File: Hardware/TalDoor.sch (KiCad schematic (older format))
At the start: 57 parts, among them J1 SI-52003-F_RJ45, J2 Screw_Terminal_01x02, J3 Conn_01x06_Male, J4 Conn_01x06_Male, P1 PocketBeagle, Q1 RK7002BM, Q2 BSS223PWH6327XTSA1, U1 DRV8837, U2 ENC28J60-I/SO, U3 PN532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

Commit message: Added 5v motor control. Updated schematic, images, BOM, PCB layout
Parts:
- added C17, C18, C19: 1uF, Capacitors_SMD:C_0603, symbol C
- added U5: CAT3200-5, TO_SOT_Packages_SMD:SOT-23-6, symbol CAT3200-5
- J2: footprint Pin_Headers:Pin_Header_Angled_1x02_Pitch2.54mm -> Pin_Headers:Pin_Header_Straight_1x02_Pitch2.54mm
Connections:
- wire segments 222 -> 237
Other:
- note added: "Motor 5v"
- note removed: "May need \nto be 5v"
- moved on the sheet: C1, C8, U1

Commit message: Started changed base on Hardware 1 build
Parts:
- removed C18, C19: 1uF, Capacitors_SMD:C_0603, symbol C
- removed J2: Screw_Terminal_01x02, Pin_Headers:Pin_Header_Straight_1x02_Pitch2.54mm, symbol Screw_Terminal_01x02
- removed U5: CAT3200-5, TO_SOT_Packages_SMD:SOT-23-6, symbol CAT3200-5
- added J2: Conn_01x02, Pin_Headers:Pin_Header_Straight_1x02_Pitch2.54mm, symbol Conn_01x02
- added U5: NCP1117-3.3_SOT223, TO_SOT_Packages_SMD:SOT-223-3_TabPin2, symbol NCP1117-3.3_SOT223
- C17: value 1uF -> 10uF; footprint Capacitors_SMD:C_0603 -> Capacitors_SMD:C_0805
- U1: footprint Housings_SON:WSON-8_1EP_2x2mm_Pitch0.5mm_ThermalVias -> TalDoor_Footprints:WSON-8_1EP_2x2mm_Pitch0.5mm_ThermalVias
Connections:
- net labels added: +5V
- wire segments 237 -> 220
- no-connect marks 12 -> 17
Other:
- note added: "3.3v Supply"
- note added: "Each VDD pin gets \n0.1uF cap to GND\n"
- note added: "MOSI/MISO may need to be changed\nper PB Testing"
- note added: "Place close \nto C12&13"
- note removed: "Each VDD pin gets 0.1uF cap to GND\n"
- note removed: "For Net conn"
- note removed: "Motor 5v"
- note removed: "VBat+"
- note removed: "Vref+"
- moved on the sheet: BZ1, C1, C10, C11, C14, C16, C2, C3, C4, C5, C6, C7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

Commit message: Updating PCB layout, unfinished
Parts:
- C15: value 1000uF -> 470uF
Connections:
- no-connect marks 17 -> 11
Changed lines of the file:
@@
 P 5900 1750
 F 0 "C15" H 5925 1850 50  0000 L CNN
-F 1 "1000uF" H 5925 1650 50  0000 L CNN
+F 1 "470uF" H 5925 1650 50  0000 L CNN
 F 2 "Capacitors_THT:CP_Radial_D10.0mm_P5.00mm" H 5900 1750 50  0001 C CNN
 F 3 "" H 5900 1750 50  0001 C CNN
@@
 	1    0    0    -1
 $EndComp
-NoConn ~ 9950 1800
-NoConn ~ 9350 1900
-NoConn ~ 9350 2200
 $Comp
 L PocketBeagle P1
@@
 	1    0    0    -1
 $EndComp
-NoConn ~ 8500 1900
-NoConn ~ 8500 2000
-NoConn ~ 8500 2200
 $Comp
 L +5V #PWR014

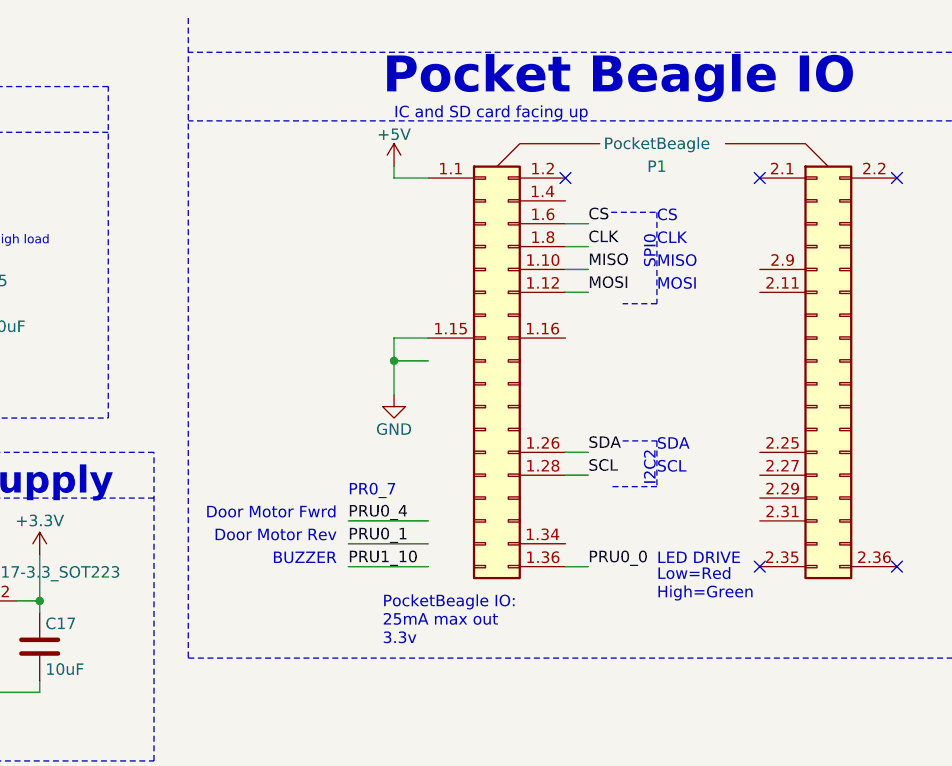
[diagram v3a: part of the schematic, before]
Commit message: Updated PCB layout for fixes from v1
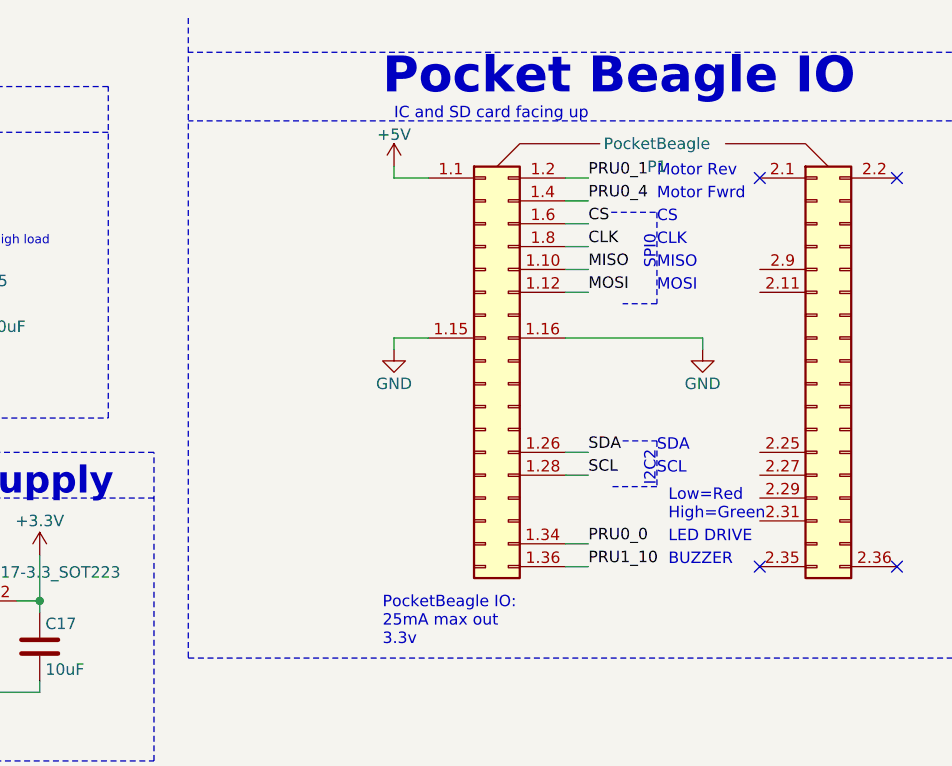
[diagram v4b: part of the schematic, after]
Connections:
- net GND: now also P1.1.16 (PIN_16)
- net PRU0_0: now also P1.1.34 (Pin_34); no longer P1.1.36 (Pin_36)
- net PRU0_1: now also P1.1.2 (Pin_2)
- net PRU0_4: now also P1.1.4 (Pin_4)
- net PRU1_10: now also P1.1.36 (Pin_36)
- no-connect marks 11 -> 10
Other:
- note added: "Motor Fwrd"
- note added: "Motor Rev"
- note removed: "Door Motor Rev"
- note removed: "PR0_7"
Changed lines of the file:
@@
 L GND #PWR06
 U 1 1 5A47602A
-P 7750 2150
-F 0 "#PWR06" H 7750 1900 50  0001 C CNN
-F 1 "GND" H 7750 2000 50  0000 C CNN
-F 2 "" H 7750 2150 50  0001 C CNN
-F 3 "" H 7750 2150 50  0001 C CNN
-	1    7750 2150
-	1    0    0    -1
-$EndComp
-Text Label 7550 2900 0    50   ~ 0
+P 7750 1950
+F 0 "#PWR06" H 7750 1700 50  0001 C CNN
+F 1 "GND" H 7750 1800 50  0000 C CNN
+F 2 "" H 7750 1950 50  0001 C CNN
+F 3 "" H 7750 1950 50  0001 C CNN
+	1    7750 1950
+	1    0    0    -1
+$EndComp
+Text Label 8600 2900 0    50   ~ 0
 PRU1_10
-Text Label 7550 2800 0    50   ~ 0
+Text Label 8600 1200 0    50   ~ 0
 PRU0_1
-Text Label 7550 2700 0    50   ~ 0
+Text Label 8600 1300 0    50   ~ 0
 PRU0_4
 Text Notes 7700 3250 0    50   ~ 0
 PocketBeagle IO:\n25mA max out\n3.3v
-Text Notes 7500 2900 2    50   ~ 0
+Text Notes 8950 2900 0    50   ~ 0
 BUZZER
-Text Notes 7500 2700 2    50   ~ 0
-Door Motor Fwrd
-Text Notes 7500 2800 2    50   ~ 0
-Door Motor Rev
+Text Notes 8900 1300 0    50   ~ 0
+Motor Fwrd
+Text Notes 8900 1200 0    50   ~ 0
+Motor Rev
 $Comp
 L LED D2
@@
 	1    0    0    1
 $EndComp
-Text Notes 8900 2900 0    50   ~ 0
+Text Notes 8950 2800 0    50   ~ 0
 LED DRIVE
-Text Label 8600 2900 0    50   ~ 0
+Text Label 8600 2800 0    50   ~ 0
 PRU0_0
 Text Label 2500 7100 0    50   ~ 0
 PRU0_4
-Text Notes 8900 3050 0    50   ~ 0
+Text Notes 8950 2700 0    50   ~ 0
 Low=Red\nHigh=Green
 $Comp
@@
 Text Label 6400 4600 1    50   ~ 0
 PRU1_10
-Text Notes 7550 2600 0    50   ~ 0
-PR0_7
 $Comp
 L LED D4
@@
 NoConn ~ 9350 1200
 NoConn ~ 9950 1200
-NoConn ~ 8500 1200
 $Bitmap
 Pos 10200 7050
@@
 Wire Wire Line
 	1350 6900 1400 6900
-Connection ~ 7750 2000
-Wire Wire Line
-	7900 2000 7750 2000
-Wire Wire Line
-	7750 1900 7750 2150
 Wire Wire Line
 	7750 1200 7750 1150
@@
 	9400 5850 9300 5850
 Wire Wire Line
-	7900 2700 7550 2700
-Wire Wire Line
-	7900 2800 7550 2800
-Wire Wire Line
-	7900 2900 7550 2900
-Wire Wire Line
 	7900 1900 7750 1900
 Wire Wire Line
@@
 Wire Wire Line
 	2400 3550 2250 3550
-Wire Wire Line
-	8500 1700 8600 1700
 Wire Wire Line
 	8500 1600 8600 1600
@@
 Text Notes 5250 3200 0    39   ~ 0
 Place close \nto C12&13
+Wire Wire Line
+	8500 2800 8600 2800
+Wire Wire Line
+	8500 1200 8600 1200
+Wire Wire Line
+	8500 1300 8600 1300
+Wire Wire Line
+	7750 1900 7750 1950
+$Comp
+L GND #PWR019
+U 1 1 5A8162E6
+P 9100 1950
+F 0 "#PWR019" H 9100 1700 50  0001 C CNN
+F 1 "GND" H 9100 1800 50  0000 C CNN
+F 2 "" H 9100 1950 50  0001 C CNN
+F 3 "" H 9100 1950 50  0001 C CNN
+	1    9100 1950
+	1    0    0    -1
+$EndComp
+Wire Wire Line
+	9100 1900 9100 1950
+Wire Wire Line
+	8500 1900 9100 1900
+Wire Wire Line
+	8500 1700 8600 1700
 $EndSCHEMATC

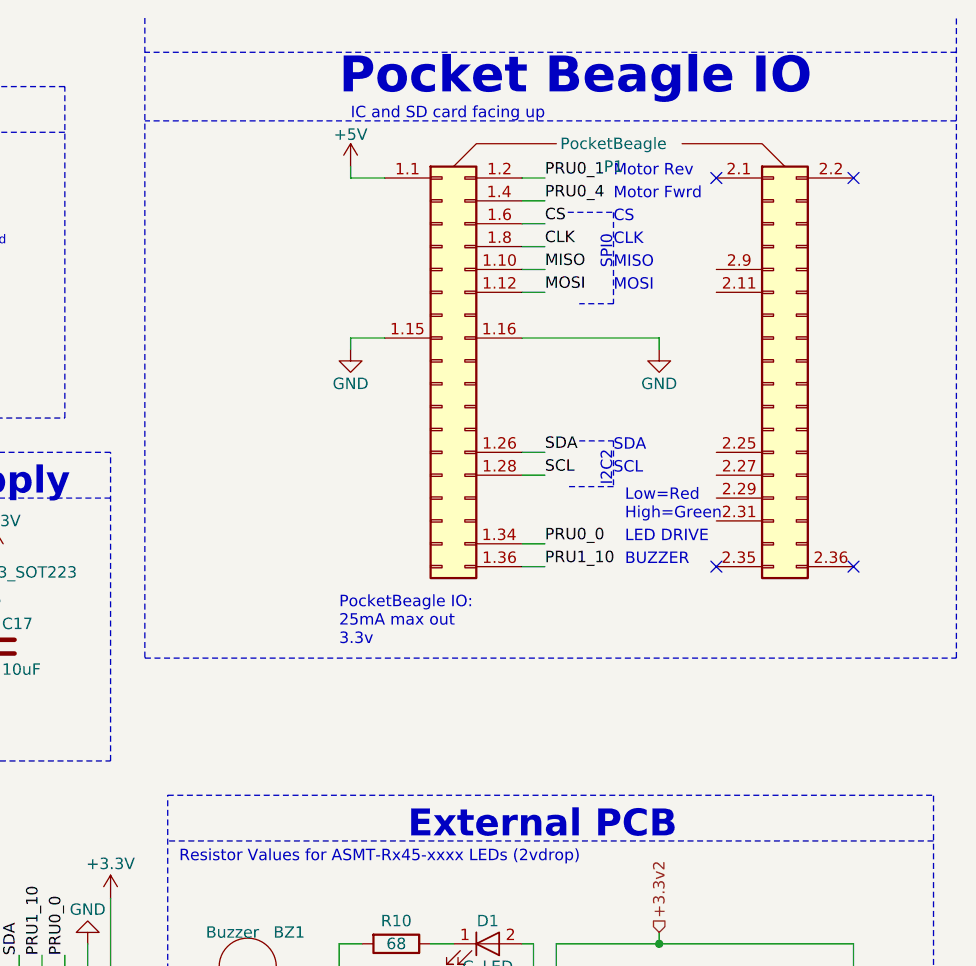
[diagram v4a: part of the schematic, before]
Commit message: Updated PCB with solder jumpers for easier developing
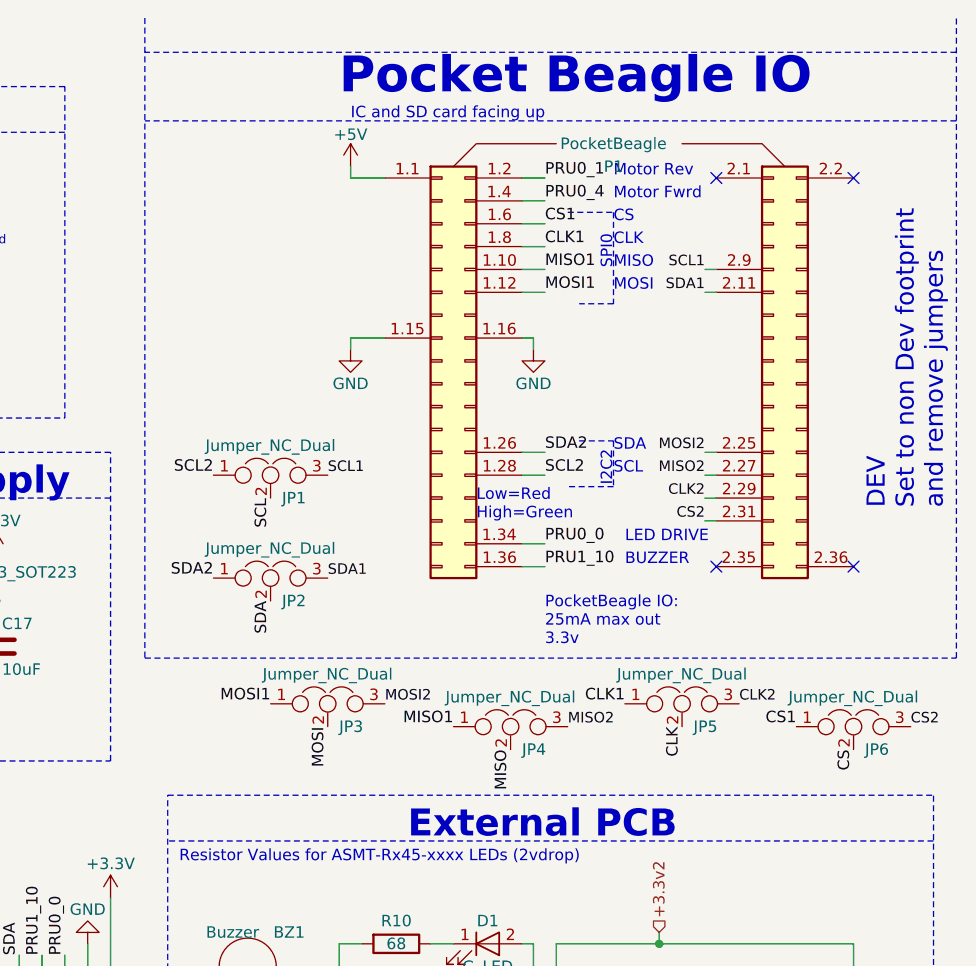
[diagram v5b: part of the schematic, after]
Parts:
- added JP1, JP2, JP3, JP4, JP5, JP6: Jumper_NC_Dual, Connectors:GS3, symbol Jumper_NC_Dual
- P1: footprint TalDoor_Footprints:PocketBeagle_TalDoor -> TalDoor_Footprints:PocketBeagle_DEV_TalDoor
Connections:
- net CLK: now also JP5.2; no longer P1.1.8 (Pin_8)
- net CS: now also JP6.2; no longer P1.1.6 (Pin_6)
- net MISO: now also JP4.2; no longer P1.1.10 (Pin_10)
- net MOSI: now also JP3.2; no longer P1.1.12 (Pin_12)
- net SCL: now also JP1.2; no longer P1.1.28 (Pin_28)
- net SDA: now also JP2.2; no longer P1.1.26 (Pin_26)
- net SDA1: now reaches P1.2.11 (Pin_11)
- net SDA1: now also JP2.3
- net MOSI2: now reaches P1.2.25 (Pin_25)
- net MOSI2: now also JP3.3
- net MISO2: now reaches P1.2.27 (Pin_27)
- net MISO2: now also JP4.3
- net CLK2: now reaches P1.2.29 (Pin_29)
- net CLK2: now also JP5.3
- net CS2: now reaches P1.2.31 (Pin_31)
- net CS2: now also JP6.3
- net SCL1: now reaches P1.2.9 (Pin_9)
- net SCL1: now also JP1.3
- new net CLK1: JP5.1, P1.1.8 (Pin_8)
- new net CS1: JP6.1, P1.1.6 (Pin_6)
- new net MISO1: JP4.1, P1.1.10 (Pin_10)
- new net MOSI1: JP3.1, P1.1.12 (Pin_12)
- new net SCL2: JP1.1, P1.1.28 (Pin_28)
- new net SDA2: JP2.1, P1.1.26 (Pin_26)
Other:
- note added: "DEV\nSet to non Dev footprint\nand remove jumpers\n"
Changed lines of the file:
@@
 CLK
 Text Label 8600 1500 0    50   ~ 0
-CLK
+CLK1
 Text Label 8600 1400 0    50   ~ 0
-CS
+CS1
 Text Label 8600 1600 0    50   ~ 0
-MISO
+MISO1
 Text Label 8600 1700 0    50   ~ 0
-MOSI
+MOSI1
 Text Notes 8900 1600 0    50   ~ 0
 MISO
@@
 MOSI
 Text Label 8600 2400 0    50   ~ 0
-SDA
+SDA2
 Text Label 8600 2500 0    50   ~ 0
-SCL
+SCL2
 $Comp
 L GND #PWR06
@@
 Text Label 8600 1300 0    50   ~ 0
 PRU0_4
-Text Notes 7700 3250 0    50   ~ 0
+Text Notes 8600 3250 0    50   ~ 0
 PocketBeagle IO:\n25mA max out\n3.3v
 Text Notes 8950 2900 0    50   ~ 0
@@
 Text Label 2500 7100 0    50   ~ 0
 PRU0_4
-Text Notes 8950 2700 0    50   ~ 0
+Text Notes 8300 2700 0    50   ~ 0
 Low=Red\nHigh=Green
 $Comp
@@
 F 0 "P1" H 8900 2850 50  0000 C CNN
 F 1 "PocketBeagle" H 8900 2950 50  0000 C CNN
-F 2 "TalDoor_Footprints:PocketBeagle_TalDoor" H 8900 1000 50  0001 C CNN
+F 2 "TalDoor_Footprints:PocketBeagle_DEV_TalDoor" H 8900 1000 50  0001 C CNN
 F 3 "" H 9450 2000 50  0001 C CNN
 	1    8900 2000
@@
 L GND #PWR019
 U 1 1 5A8162E6
-P 9100 1950
-F 0 "#PWR019" H 9100 1700 50  0001 C CNN
-F 1 "GND" H 9100 1800 50  0000 C CNN
-F 2 "" H 9100 1950 50  0001 C CNN
-F 3 "" H 9100 1950 50  0001 C CNN
-	1    9100 1950
-	1    0    0    -1
-$EndComp
-Wire Wire Line
-	9100 1900 9100 1950
-Wire Wire Line
-	8500 1900 9100 1900
+P 8550 1950
+F 0 "#PWR019" H 8550 1700 50  0001 C CNN
+F 1 "GND" H 8550 1800 50  0000 C CNN
+F 2 "" H 8550 1950 50  0001 C CNN
+F 3 "" H 8550 1950 50  0001 C CNN
+	1    8550 1950
+	1    0    0    -1
+$EndComp
 Wire Wire Line
 	8500 1700 8600 1700
+$Comp
+L Jumper_NC_Dual JP2
+U 1 1 5A819C75
+P 7400 2950
+F 0 "JP2" H 7450 2850 50  0000 L CNN
+F 1 "Jumper_NC_Dual" H 7400 3050 50  0000 C BNN
+F 2 "Connectors:GS3" H 7400 2950 50  0001 C CNN
+F 3 "" H 7400 2950 50  0001 C CNN
+	1    7400 2950
+	1    0    0    -1
+$EndComp
+Text Notes 10350 2650 1    79   ~ 0
+DEV\nSet to non Dev footprint\nand remove jumpers\n
+Wire Wire Line
+	8500 1900 8550 1900
+Wire Wire Line
+	8550 1900 8550 1950
+Wire Wire Line
+	9350 2700 9300 2700
+Wire Wire Line
+	9350 2600 9300 2600
+Wire Wire Line
+	9350 2500 9300 2500
+Wire Wire Line
+	9350 2400 9300 2400
+Wire Wire Line
+	9300 1600 9350 1600
+Wire Wire Line
+	9350 1700 9300 1700
+Text Label 9300 1700 2    46   ~ 0
+SDA1
+Text Label 9300 1600 2    46   ~ 0
+SCL1
+$Comp
+L Jumper_NC_Dual JP1
+U 1 1 5A867D5F
+P 7400 2500
+F 0 "JP1" H 7450 2400 50  0000 L CNN
+F 1 "Jumper_NC_Dual" H 7400 2600 50  0000 C BNN
+F 2 "Connectors:GS3" H 7400 2500 50  0001 C CNN
+F 3 "" H 7400 2500 50  0001 C CNN
+	1    7400 2500
+	1    0    0    -1
+$EndComp
+$Comp
+L Jumper_NC_Dual JP4
+U 1 1 5A867E50
+P 8450 3600
+F 0 "JP4" H 8500 3500 50  0000 L CNN
+F 1 "Jumper_NC_Dual" H 8450 3700 50  0000 C BNN
+F 2 "Connectors:GS3" H 8450 3600 50  0001 C CNN
+F 3 "" H 8450 3600 50  0001 C CNN
+	1    8450 3600
+	1    0    0    -1
+$EndComp
+$Comp
+L Jumper_NC_Dual JP5
+U 1 1 5A867F28
+P 9200 3500
+F 0 "JP5" H 9250 3400 50  0000 L CNN
+F 1 "Jumper_NC_Dual" H 9200 3600 50  0000 C BNN
+F 2 "Connectors:GS3" H 9200 3500 50  0001 C CNN
+F 3 "" H 9200 3500 50  0001 C CNN
+	1    9200 3500
+	1    0    0    -1
+$EndComp
+$Comp
+L Jumper_NC_Dual JP6
+U 1 1 5A868009
+P 9950 3600
+F 0 "JP6" H 10000 3500 50  0000 L CNN
+F 1 "Jumper_NC_Dual" H 9950 3700 50  0000 C BNN
+F 2 "Connectors:GS3" H 9950 3600 50  0001 C CNN
+F 3 "" H 9950 3600 50  0001 C CNN
+	1    9950 3600
+	1    0    0    -1
+$EndComp
+$Comp
+L Jumper_NC_Dual JP3
+U 1 1 5A868BD7
+P 7650 3500
+F 0 "JP3" H 7700 3400 50  0000 L CNN
+F 1 "Jumper_NC_Dual" H 7650 3600 50  0000 C BNN
+F 2 "Connectors:GS3" H 7650 3500 50  0001 C CNN
+F 3 "" H 7650 3500 50  0001 C CNN
+	1    7650 3500
+	1    0    0    -1
+$EndComp
+Text Label 9300 2400 2    46   ~ 0
+MOSI2
+Text Label 9300 2500 2    46   ~ 0
+MISO2
+Text Label 9300 2600 2    46   ~ 0
+CLK2
+Text Label 9300 2700 2    46   ~ 0
+CS2
+Text Label 10200 3600 0    46   ~ 0
+CS2
+Text Label 9450 3500 0    46   ~ 0
+CLK2
+Text Label 8700 3600 0    46   ~ 0
+MISO2
+Text Label 7900 3500 0    46   ~ 0
+MOSI2
+Text Label 7650 2950 0    46   ~ 0
+SDA1
+Text Label 7650 2500 0    46   ~ 0
+SCL1
+Text Label 7400 3050 3    50   ~ 0
+SDA
+Text Label 7400 2600 3    50   ~ 0
+SCL
+Text Label 7650 3600 3    50   ~ 0
+MOSI
+Text Label 8450 3700 3    50   ~ 0
+MISO
+Text Label 9200 3600 3    50   ~ 0
+CLK
+Text Label 9950 3700 3    50   ~ 0
+CS
+Text Label 7150 2950 2    50   ~ 0
+SDA2
+Text Label 7150 2500 2    50   ~ 0
+SCL2
+Text Label 7400 3500 2    50   ~ 0
+MOSI1
+Text Label 8950 3500 2    50   ~ 0
+CLK1
+Text Label 8200 3600 2    50   ~ 0
+MISO1
+Text Label 9700 3600 2    50   ~ 0
+CS1
 $EndSCHEMATC
